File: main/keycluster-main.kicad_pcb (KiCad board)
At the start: 2 copper layers, 45.1 x 52.6 mm, 33 parts, among them P2 CONN_5, P7 CONN_10, P8 CONN_7, SW1 S01_Socket, SW2 S01_Socket, SW3 S01_Socket, SW4 CMI126603D08, SW6 CMI126603D08, U1 MKL03Z32VFK4, U2 IS31FL3199, U4 ESD

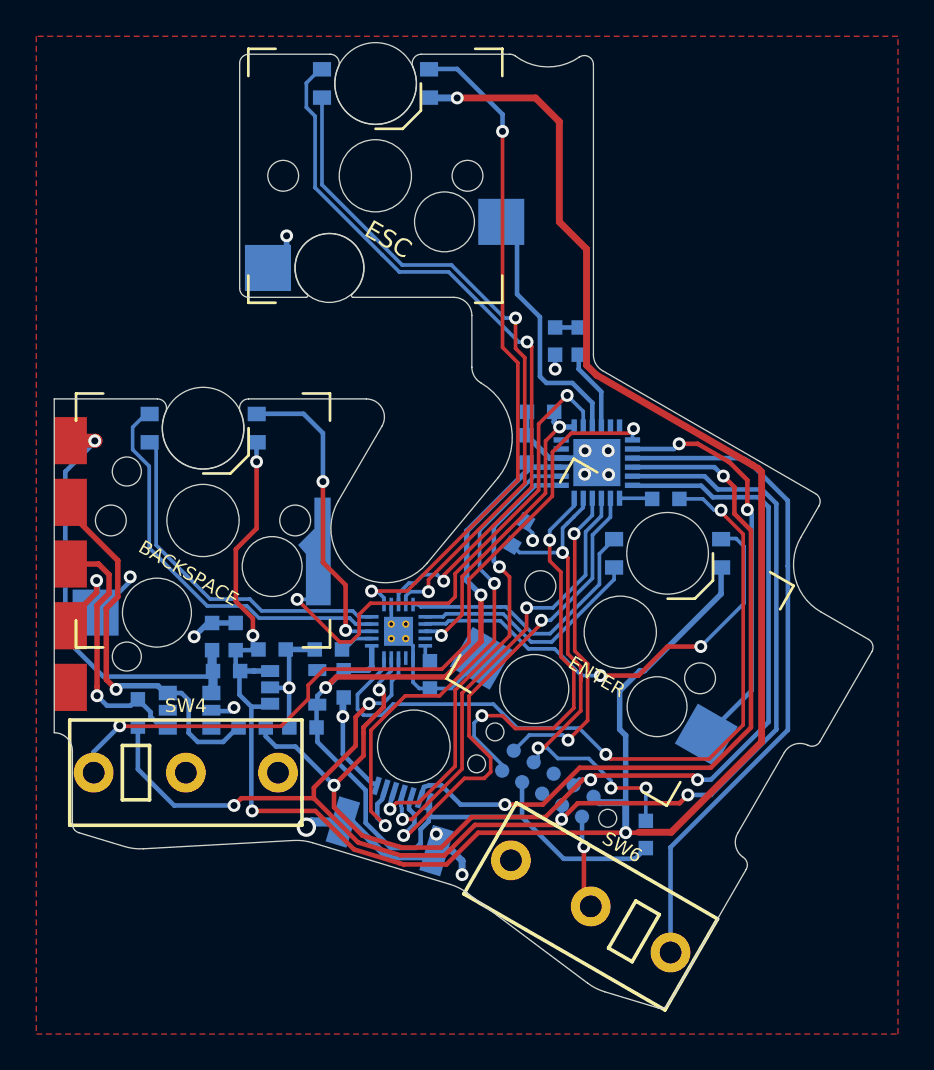
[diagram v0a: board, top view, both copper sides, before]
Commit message: Readd positioning holes.
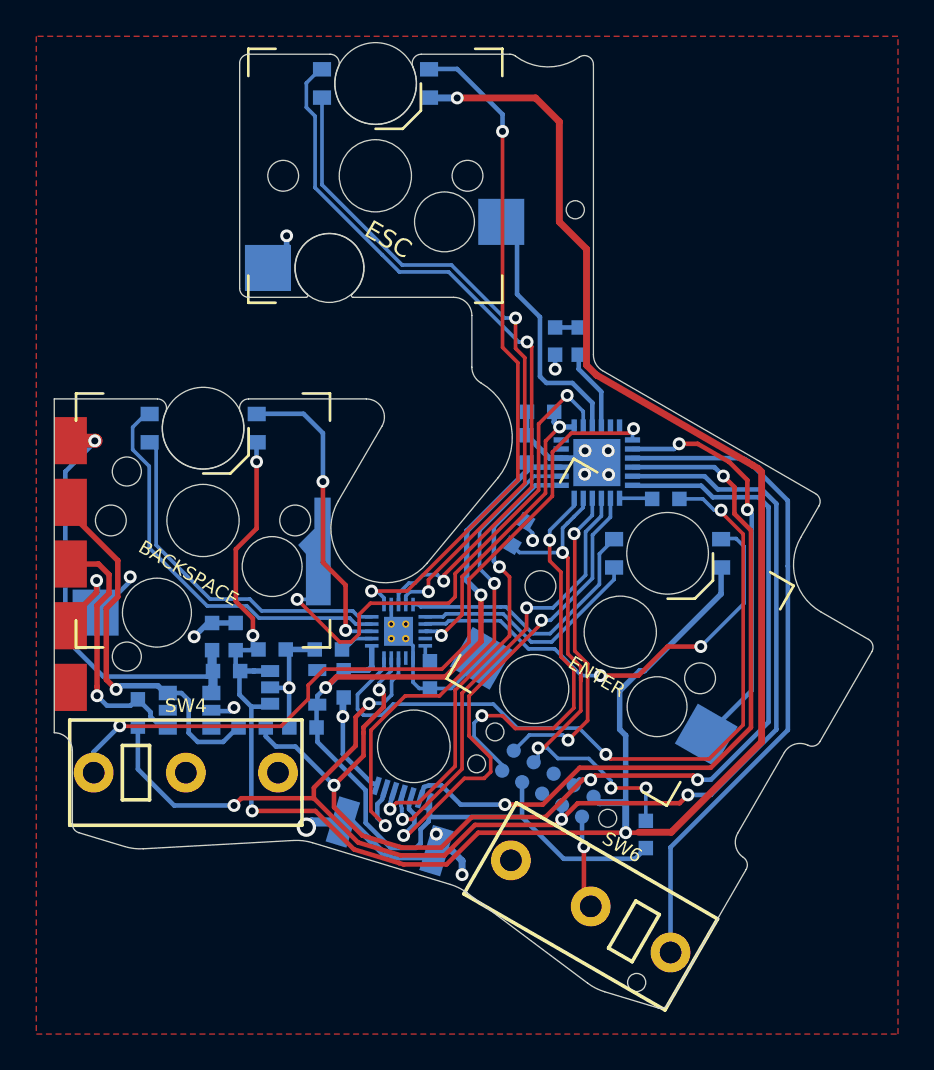
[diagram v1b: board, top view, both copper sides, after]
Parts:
- added hole: 1.0mm, UGL:hole_1.0mm, F.Cu at (153.7, 89.6)
- added hole: 1.0mm, UGL:hole_1.0mm, F.Cu at (157.1, 132.2)

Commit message: Add back UHK logo.
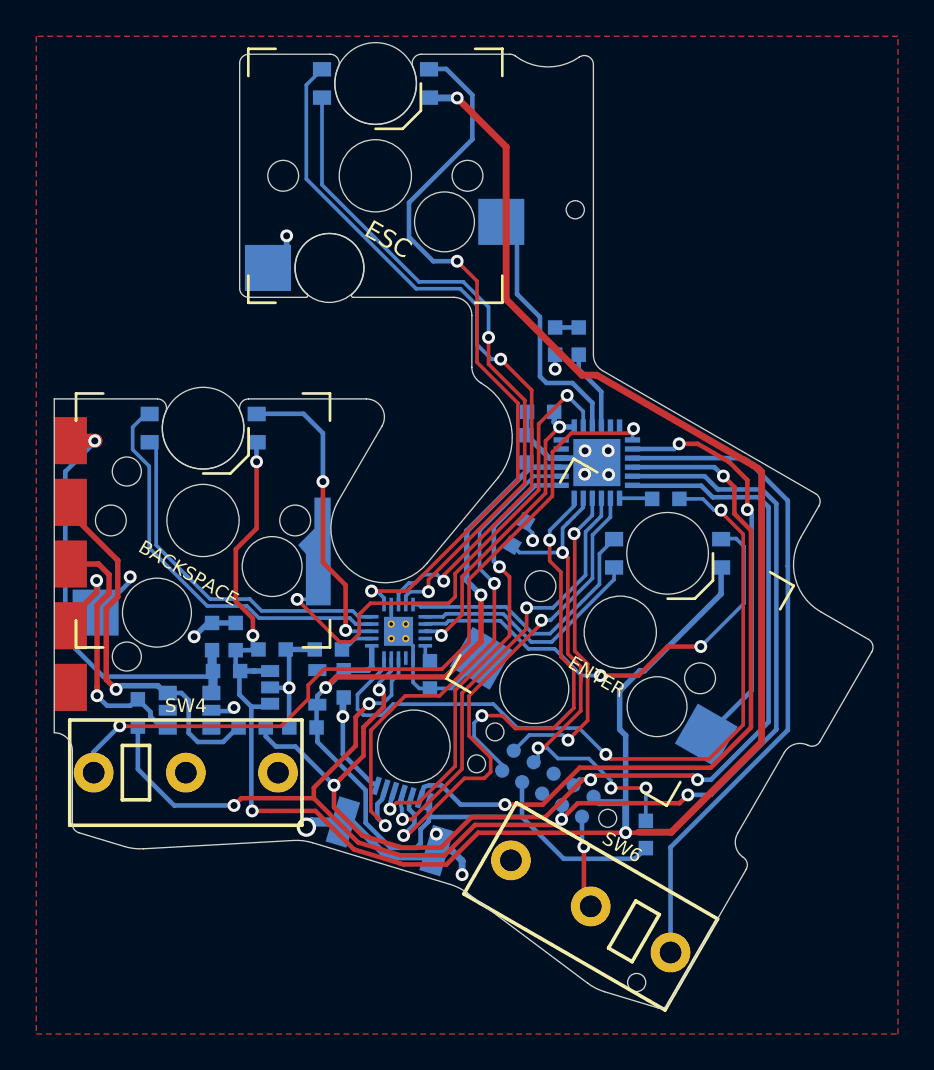
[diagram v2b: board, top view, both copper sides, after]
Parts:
- added G***: LOGO, UGL:UHK_Logo_12x3.4_mm, F.Cu at (152.2, 88.4)
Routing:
- net Net-(D1-Pad3): track 37.4 -> 40.7 mm
- net +5V: track 124.2 -> 122.1 mm
- net Net-(D1-Pad2): track 37.8 -> 37.3 mm

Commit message: Update netlist and board.
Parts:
- R3: value 100k -> 5.1K
- R4: value 100k -> 20K
- R5: value 10k -> 5.1K

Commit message: Rename the test LED reference designator to D2.
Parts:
- renumbered D1 to D11, D2 to D12, D3 to D13, D7 to D2

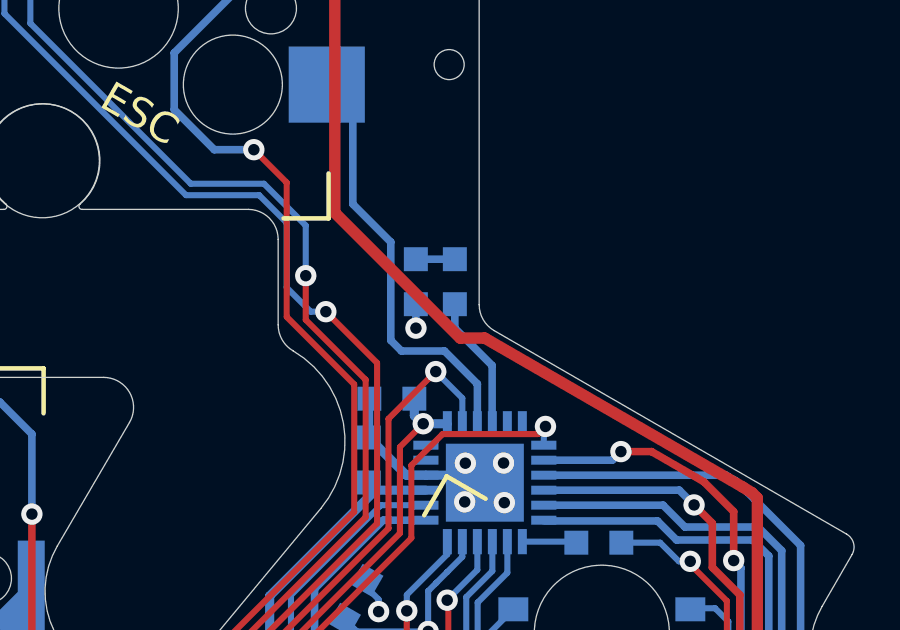
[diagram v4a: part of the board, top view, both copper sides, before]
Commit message: Add test LED section.
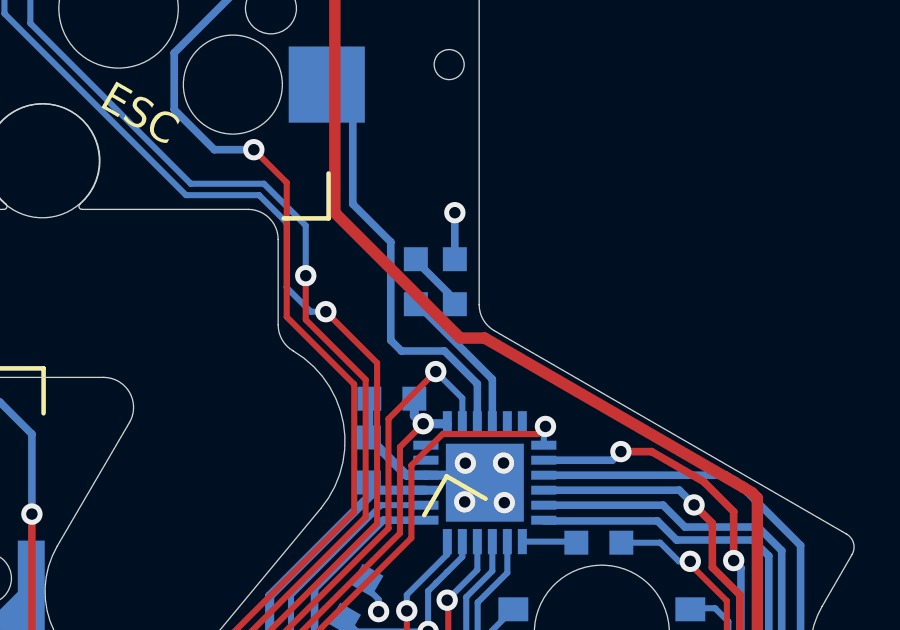
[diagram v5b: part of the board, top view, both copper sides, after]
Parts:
- moved D2 1.30 mm to (153.9, 96.8), turned to 270 degrees
- moved R2 1.30 mm to (152.6, 96.8)
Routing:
- net GND: track 54.6 -> 55.3 mm
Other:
- board text added: "TEST LED"
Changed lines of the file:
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@@
   (general
     (thickness 1.6)
-    (drawings 94)
+    (drawings 99)
     (tracks 702)
     (zones 0)
@@
     (37 F.SilkS user)
     (38 B.Mask user)
-    (39 F.Mask user)
+    (39 F.Mask user hide)
     (40 Dwgs.User user)
     (41 Cmts.User user)
@@
   )
   (setup
-    (last_trace_width 0.2032)
+    (last_trace_width 0.254)
     (user_trace_width 0.2032)
     (user_trace_width 0.254)
@@
   )
   (module UGL:SM0603_Diode (layer B.Cu)
-    (at 152.609512 96.810302 90)
+    (at 153.909512 96.810302 270)
     (attr virtual)
-    (fp_text reference D2 (at 2.2 0 90) (layer B.SilkS)
-      (effects (font (size 0.75 0.75) (thickness 0.15)) (justify mirror))
-    )
-    (fp_text value LED (at 4.2 0 270) (layer B.SilkS)
+    (fp_text reference D2 (at -3.5 -0.2 90) (layer B.SilkS)
+      (effects (font (size 0.75 0.75) (thickness 0.15)) (justify mirror))
+    )
+    (fp_text value LED (at -5.7 -0.2 90) (layer B.SilkS)
       (effects (font (size 0.75 0.75) (thickness 0.15)) (justify mirror))
     )
     (fp_line (start -1.6 0.4) (end -1.6 -0.4) (layer B.SilkS) (width 0.15))
-    (pad 1 smd rect (at -0.75 0 90) (size 0.8 0.8) (layers B.Cu B.Paste B.Mask)
-      (net 1 GND))
-    (pad 2 smd rect (at 0.75 0 90) (size 0.8 0.8) (layers B.Cu B.Paste B.Mask)
+    (pad 2 smd rect (at 0.75 0 270) (size 0.8 0.8) (layers B.Cu B.Mask)
       (net 9 /TEST_LED_R))
+    (pad 1 smd rect (at -0.75 0 270) (size 0.8 0.8) (layers B.Cu B.Mask)
+      (net 1 GND))
     (model smd\resistors\R0603.wrl
       (offset (xyz 0 0 0.02540000082496551))
@@
       (effects (font (size 0.75 0.75) (thickness 0.15)) (justify mirror))
     )
+    (fp_line (start -2.8 3.55) (end -2.8 3) (layer B.SilkS) (width 0.15))
+    (fp_line (start 2.05 3.55) (end 2.8 3.55) (layer B.SilkS) (width 0.15))
+    (fp_line (start 2.8 3.55) (end 2.8 3) (layer B.SilkS) (width 0.15))
+    (fp_line (start -2.8 0) (end 2.8 0) (layer Margin) (width 0.15))
     (fp_line (start -2.8 3.55) (end -2.05 3.55) (layer B.SilkS) (width 0.15))
-    (fp_line (start -2.8 0) (end 2.8 0) (layer Margin) (width 0.15))
-    (fp_line (start 2.8 3.55) (end 2.8 3) (layer B.SilkS) (width 0.15))
-    (fp_line (start 2.05 3.55) (end 2.8 3.55) (layer B.SilkS) (width 0.15))
-    (fp_line (start -2.8 3.55) (end -2.8 3) (layer B.SilkS) (width 0.15))
+    (pad 7 smd rect (at 1.5 4 163) (size 0.3 1) (layers B.Cu B.Paste B.Mask)
+      (net 1 GND) (clearance 0.1778))
+    (pad 6 smd rect (at 1 4 163) (size 0.3 1) (layers B.Cu B.Paste B.Mask)
+      (net 22 /SW5) (clearance 0.1778))
+    (pad 1 smd rect (at -1.5 4 163) (size 0.3 1) (layers B.Cu B.Paste B.Mask)
+      (net 6 +3V3) (clearance 0.1778))
+    (pad "" smd rect (at -2.7 1.55 163) (size 1.2 2.6) (layers B.Cu B.Paste B.Mask)
+      (net 1 GND))
+    (pad 4 smd rect (at 0 4 163) (size 0.3 1) (layers B.Cu B.Paste B.Mask)
+      (net 13 /TB_UP) (clearance 0.1778))
+    (pad 3 smd rect (at -0.5 4 163) (size 0.3 1) (layers B.Cu B.Paste B.Mask)
+      (net 16 /TB_DOWN) (clearance 0.1778))
+    (pad "" smd rect (at 2.7 1.55 163) (size 1.2 2.6) (layers B.Cu B.Paste B.Mask)
+      (net 1 GND))
+    (pad 5 smd rect (at 0.5 4 163) (size 0.3 1) (layers B.Cu B.Paste B.Mask)
+      (net 14 /TB_RIGHT) (clearance 0.1778))
     (pad 2 smd rect (at -1 4 163) (size 0.3 1) (layers B.Cu B.Paste B.Mask)
       (net 15 /TB_LEFT) (clearance 0.1778))
-    (pad 5 smd rect (at 0.5 4 163) (size 0.3 1) (layers B.Cu B.Paste B.Mask)
-      (net 14 /TB_RIGHT) (clearance 0.1778))
-    (pad "" smd rect (at 2.7 1.55 163) (size 1.2 2.6) (layers B.Cu B.Paste B.Mask)
-      (net 1 GND))
-    (pad 3 smd rect (at -0.5 4 163) (size 0.3 1) (layers B.Cu B.Paste B.Mask)
-      (net 16 /TB_DOWN) (clearance 0.1778))
-    (pad 4 smd rect (at 0 4 163) (size 0.3 1) (layers B.Cu B.Paste B.Mask)
-      (net 13 /TB_UP) (clearance 0.1778))
-    (pad "" smd rect (at -2.7 1.55 163) (size 1.2 2.6) (layers B.Cu B.Paste B.Mask)
-      (net 1 GND))
-    (pad 1 smd rect (at -1.5 4 163) (size 0.3 1) (layers B.Cu B.Paste B.Mask)
-      (net 6 +3V3) (clearance 0.1778))
-    (pad 6 smd rect (at 1 4 163) (size 0.3 1) (layers B.Cu B.Paste B.Mask)
-      (net 22 /SW5) (clearance 0.1778))
-    (pad 7 smd rect (at 1.5 4 163) (size 0.3 1) (layers B.Cu B.Paste B.Mask)
-      (net 1 GND) (clearance 0.1778))
   )
   (module UGL:SM0603 (layer B.Cu)
@@
   )
   (module UGL:SM0603 (layer B.Cu)
-    (at 153.909512 96.810302 270)
+    (at 152.609512 96.810302 270)
     (attr virtual)
-    (fp_text reference R2 (at -2.2 0 270) (layer B.SilkS)
-      (effects (font (size 0.75 0.75) (thickness 0.15)) (justify mirror))
-    )
-    (fp_text value 330 (at -4.2 0 90) (layer B.SilkS)
+    (fp_text reference R2 (at -3.5 -0.4 270) (layer B.SilkS)
+      (effects (font (size 0.75 0.75) (thickness 0.15)) (justify mirror))
+    )
+    (fp_text value 330 (at -5.6 -0.4 90) (layer B.SilkS)
       (effects (font (size 0.75 0.75) (thickness 0.15)) (justify mirror))
     )
     (fp_line (start -0.4 0.5) (end 0.4 0.5) (layer B.SilkS) (width 0.127))
     (fp_line (start 0.4 -0.5) (end -0.4 -0.5) (layer B.SilkS) (width 0.127))
-    (pad 2 smd rect (at 0.75 0 270) (size 0.8 0.8) (layers B.Cu B.Paste B.Mask)
+    (pad 2 smd rect (at 0.75 0 270) (size 0.8 0.8) (layers B.Cu B.Mask)
       (net 10 /TEST_LED))
-    (pad 1 smd rect (at -0.75 0 270) (size 0.8 0.8) (layers B.Cu B.Paste B.Mask)
+    (pad 1 smd rect (at -0.75 0 270) (size 0.8 0.8) (layers B.Cu B.Mask)
       (net 9 /TEST_LED_R))
     (model smd\resistors\R0603.wrl
@@
       (rotate (xyz 0 0 0))
     )
+  )
+  (gr_line (start 152.109512 98.310302) (end 155.009512 98.310302) (layer B.SilkS) (width 0.15))
+  (gr_line (start 151.009512 97.210302) (end 152.109512 98.310302) (layer B.SilkS) (width 0.15))
+  (gr_line (start 151.009512 91.810302) (end 151.009512 97.210302) (layer B.SilkS) (width 0.15))
+  (gr_line (start 154.609512 89.910302) (end 151.209512 89.910302) (layer B.SilkS) (width 0.15))
+  (gr_text "TEST LED" (at 151.809512 92.710302 90) (layer B.SilkS)
+    (effects (font (size 0.75 0.75) (thickness 0.15)) (justify mirror))
   )
   (gr_text "PCB ID:\nkeycluster_main_2.4.0" (at 162.493312 121.437542 60) (layer B.SilkS)
@@
   (segment (start 150.984512 106.760783) (end 150.984512 107.017902) (width 0.2032) (layer B.Cu) (net 1))
   (segment (start 150.984512 107.017902) (end 151.368112 107.401502) (width 0.2032) (layer B.Cu) (net 1))
-  (segment (start 152.612712 98.359102) (end 152.609512 98.355902) (width 0.254) (layer B.Cu) (net 1))
-  (via (at 152.612712 98.359102) (size 0.7112) (drill 0.381) (layers F.Cu B.Cu) (net 1))
-  (segment (start 152.609512 97.560302) (end 152.612712 98.359102) (width 0.254) (layer B.Cu) (net 1))
+  (via (at 153.909512 94.510302) (size 0.7112) (drill 0.381) (layers F.Cu B.Cu) (net 1))
+  (segment (start 153.909512 96.060302) (end 153.909512 94.510302) (width 0.254) (layer B.Cu) (net 1))
   (segment (start 127.359516 116.410306) (end 127.359516 116.360302) (width 0.3048) (layer B.Cu) (net 2))
   (via (at 127.359516 116.360302) (size 0.7112) (drill 0.381) (layers F.Cu B.Cu) (net 2))
@@
   (segment (start 161.197912 121.828702) (end 159.927912 121.828702) (width 0.254) (layer B.Cu) (net 8))
   (segment (start 164.804722 105.774841) (end 164.804722 118.221892) (width 0.254) (layer B.Cu) (net 8))
-  (segment (start 152.609512 96.060302) (end 153.909512 96.060302) (width 0.254) (layer B.Cu) (net 9))
-  (segment (start 153.909512 98.360502) (end 153.909512 97.560302) (width 0.254) (layer B.Cu) (net 10))
-  (segment (start 155.152712 101.559502) (end 155.152712 99.603702) (width 0.254) (layer B.Cu) (net 10))
-  (segment (start 155.152712 99.603702) (end 153.909512 98.360502) (width 0.254) (layer B.Cu) (net 10))
+  (segment (start 152.609512 96.060302) (end 152.659512 96.060302) (width 0.254) (layer B.Cu) (net 9))
+  (segment (start 152.609512 96.060302) (end 152.609512 96.110302) (width 0.254) (layer B.Cu) (net 9))
+  (segment (start 152.609512 96.110302) (end 153.709512 97.210302) (width 0.254) (layer B.Cu) (net 9))
+  (segment (start 155.159512 101.545302) (end 155.159512 100.060302) (width 0.254) (layer B.Cu) (net 10))
+  (segment (start 155.159512 100.060302) (end 152.909512 97.810302) (width 0.254) (layer B.Cu) (net 10))
   (via (at 152.307912 107.782502) (size 0.7112) (drill 0.381) (layers F.Cu B.Cu) (net 11))
   (segment (start 149.692307 120.490228) (end 149.692307 120.178297) (width 0.2032) (layer B.Cu) (net 11))
